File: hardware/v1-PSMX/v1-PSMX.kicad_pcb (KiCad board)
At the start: 2 copper layers, 91.4 x 48.8 mm, 36 parts, among them IC1 MAX98357AETE+T (L), IC2 MAX98357AETE+T (R), J1 +5v_POWER, J2 Conn_01x04, J3 10118192-0002LF, J4 Serial_Breakout, U1 ESP32-S3-WROOM-1, U2 AZ1084-3.3

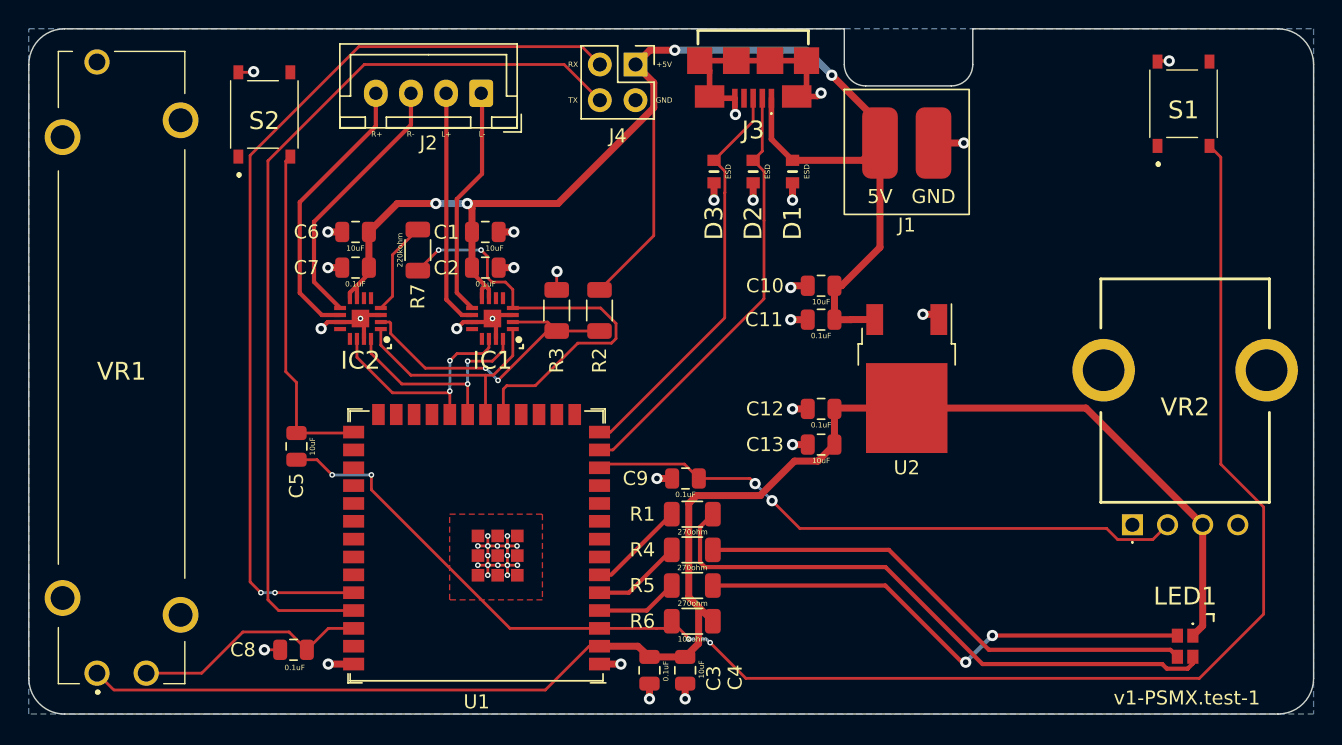
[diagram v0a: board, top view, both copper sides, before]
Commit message: Updated track widths to work with 1oz
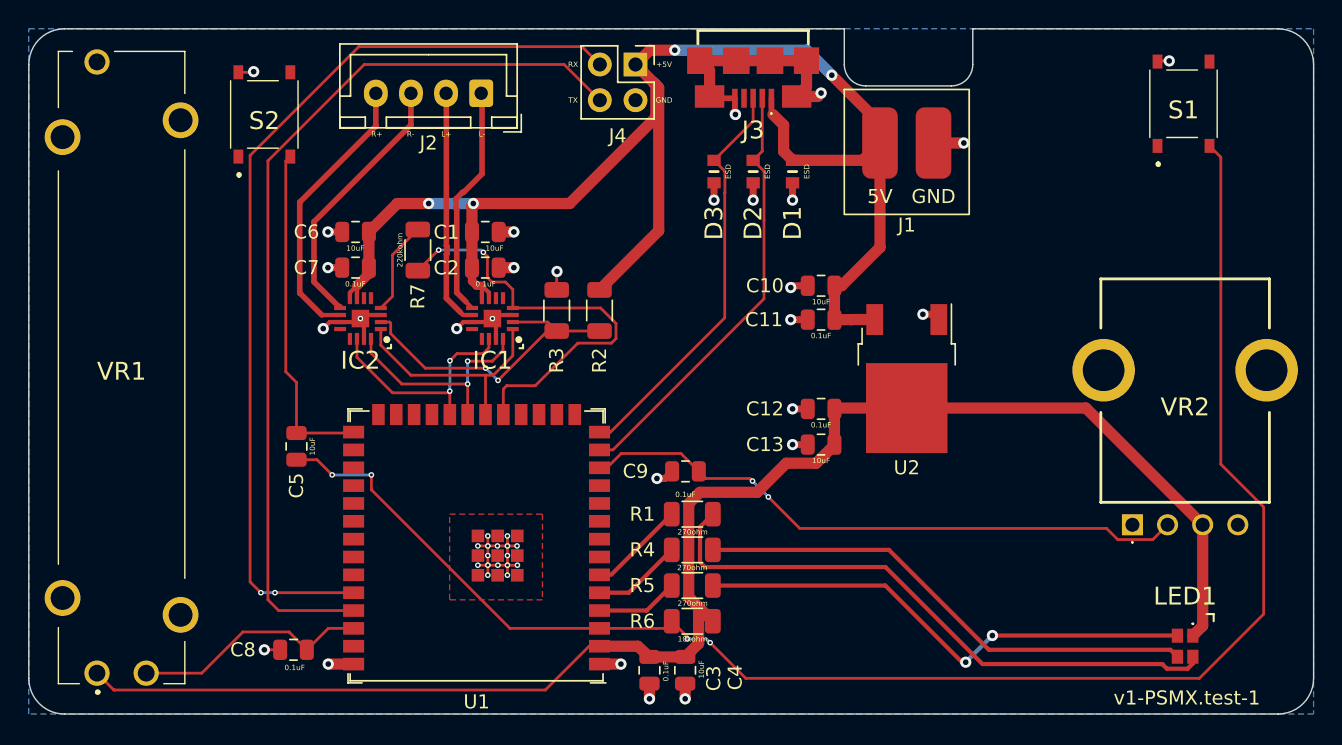
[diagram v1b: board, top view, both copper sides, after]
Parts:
- moved C9 0.51 mm to (145.3, 111.8)
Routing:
- net +5V: track 108.6 -> 109.6 mm
- net /V_POT_GPIO08: track 43.2 -> 43.8 mm

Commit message: added screw hole, misc improvements
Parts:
- added ?: , , F.Cu at (170.2, 83.4)
- added REF**: MountingHole_3.2mm_M3_Pad, MountingHole:MountingHole_3.2mm_M3_Pad, F.Cu at (105.2, 104.6)
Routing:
- net GND: track 67.9 -> 72.1 mm, vias 44 -> 49
- net /RESET: track 113.2 -> 114.9 mm
- net +5V: track 109.6 -> 108.4 mm
